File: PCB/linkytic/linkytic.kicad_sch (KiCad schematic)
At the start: 14 parts, among them U1 M5333B, U2 cc2530

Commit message: v0
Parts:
- removed C? (x2): 27pF, Capacitor_SMD:C_0603_1608Metric, symbol Device:C
- removed U2: cc2530, Package_DFN_QFN:HVQFN-40-1EP_6x6mm_P0.5mm_EP4.1x4.1mm, symbol cc2530:cc2530
- removed Y?: Crystal_GND24, symbol Device:Crystal_GND24
- added JP?: Jumper_2_Open, symbol Jumper:Jumper_2_Open
- added U?: CC_debugger, Connector_IDC:IDC-Header_2x05_P2.54mm_Vertical, symbol cc_debugger:CC_debugger
- added U?: E18-MS1-PCB, RF_Module:E18-MS1-PCB, symbol RF_Module:E18-MS1-PCB
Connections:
- net 3v3: now also JP?.1 (A)
- net GND: now also U?.1 (GND), U?.1 (GND)
- net at OC?.4, R?.1: now also U?.21 (P0.2)
- new net: JP?.2 (B), U?.2 (VDD), U?.9 (VCC)
- new net: U?.3 (P2.2), U?.3 (debug_clock_P2.2)
- new net: U?.4 (DD_P2.1), U?.4 (P2.1)
- new net: U?.24 (~{RESET}), U?.7 (RST)

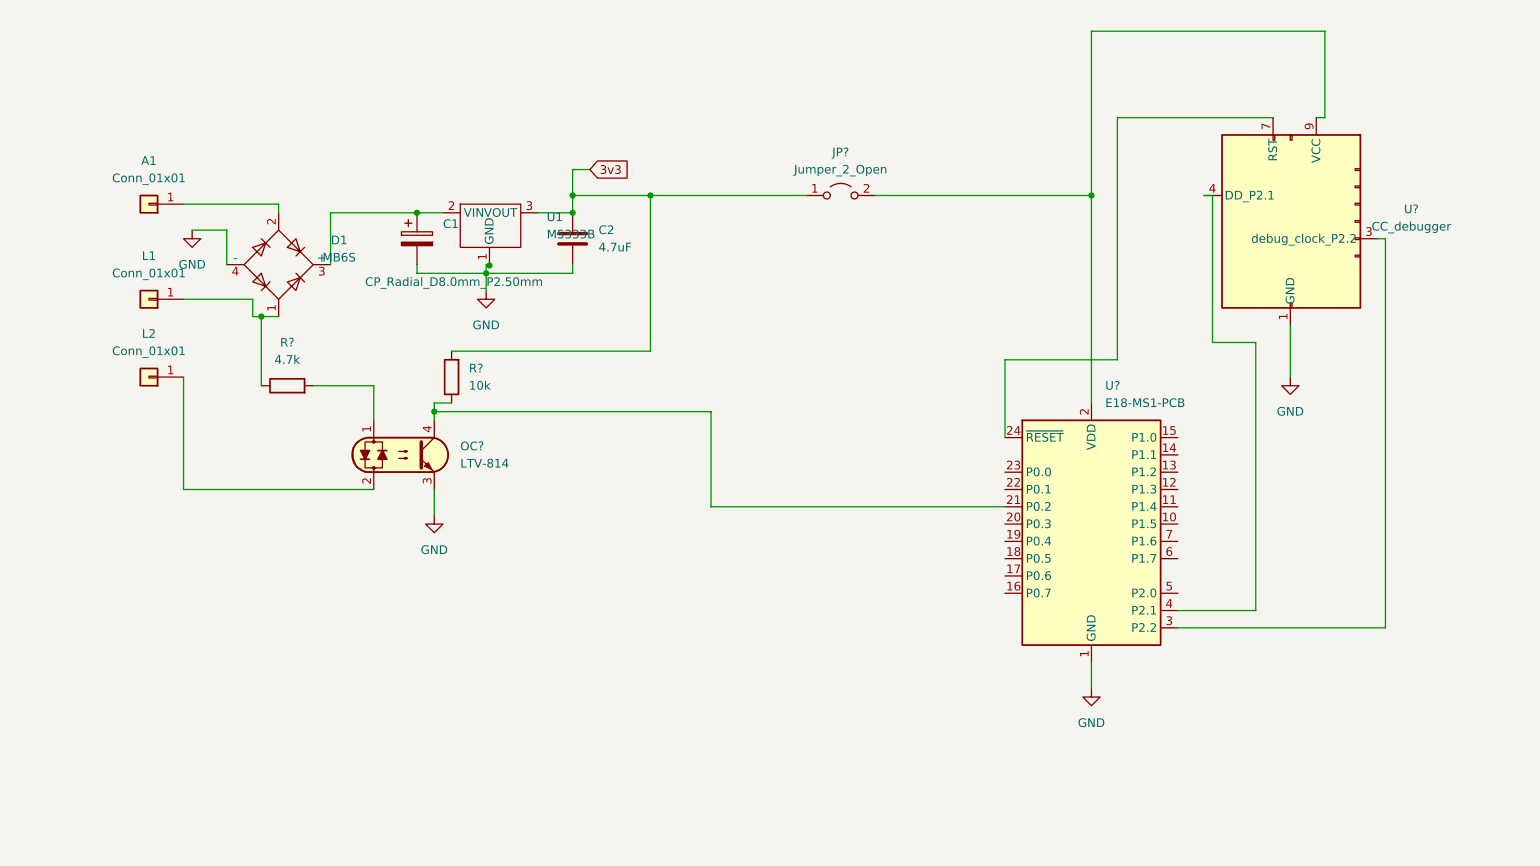
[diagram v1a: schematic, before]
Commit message: Update with thermometre on same board
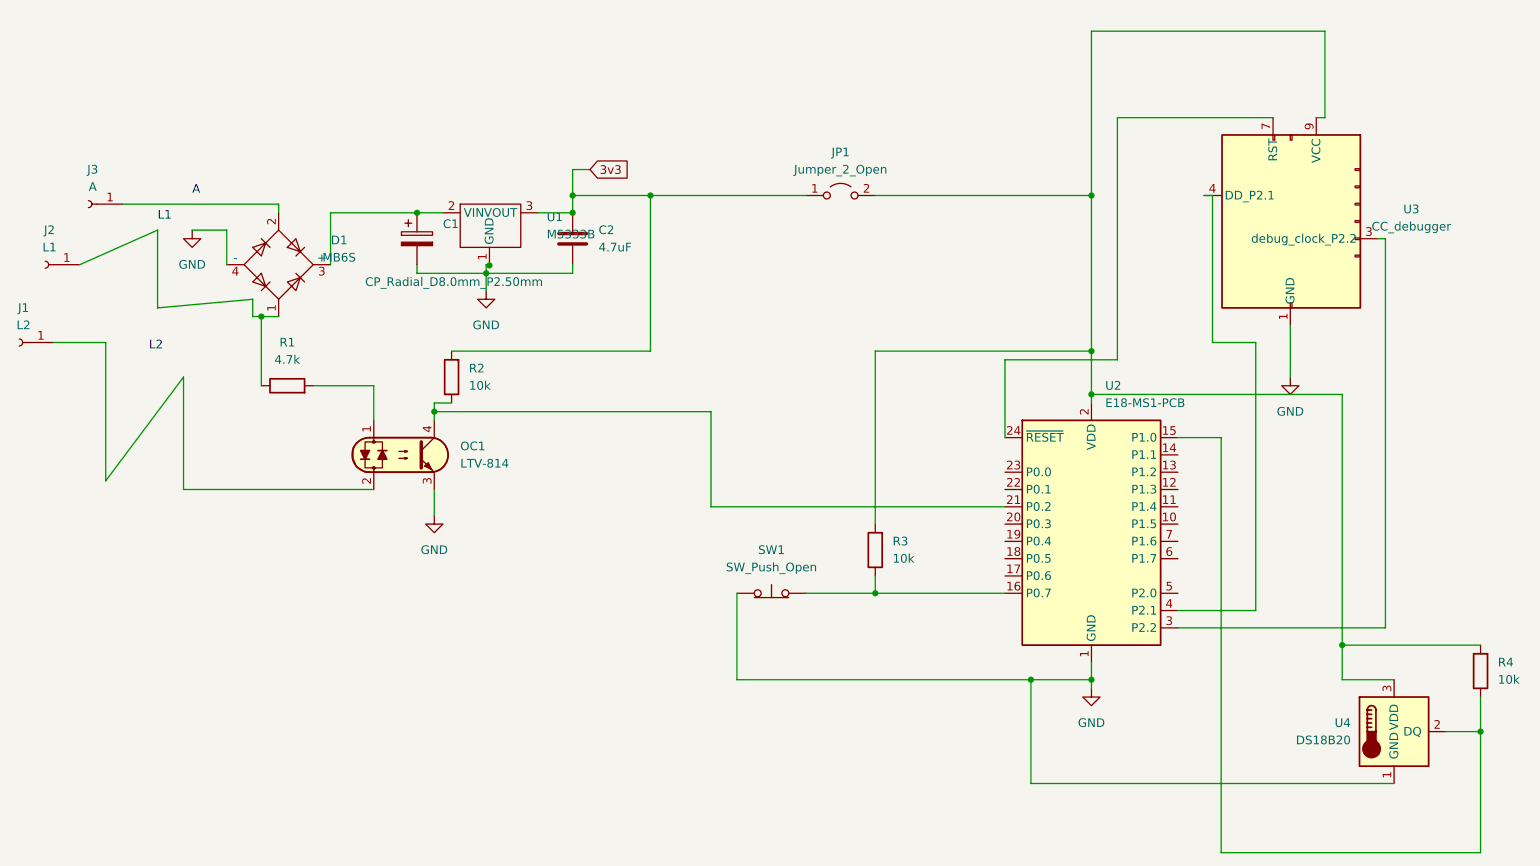
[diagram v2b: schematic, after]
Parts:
- removed A1, L1, L2: Conn_01x01, Connector_Pin:Pin_D1.0mm_L10.0mm, symbol Connector_Generic:Conn_01x01
- added J1: L2, TestPoint:TestPoint_Loop_D2.54mm_Drill1.5mm_Beaded, symbol Connector:Conn_01x01_Female
- added J2: L1, TestPoint:TestPoint_Loop_D2.54mm_Drill1.5mm_Beaded, symbol Connector:Conn_01x01_Female
- added J3: A, TestPoint:TestPoint_Loop_D2.54mm_Drill1.5mm_Beaded, symbol Connector:Conn_01x01_Female
- added R3, R4: 10k, Resistor_SMD:R_0603_1608Metric_Pad0.98x0.95mm_HandSolder, symbol Device:R
- added SW1: SW_Push_Open, Library:interrupteur, symbol Switch:SW_Push_Open
- added U4: DS18B20, Package_TO_SOT_THT:TO-92_Inline, symbol Sensor_Temperature:DS18B20
- JP1: renamed from JP?; footprint (none) -> Jumper_AKL:Jumper_P2.54mm_D0.7mm
- R1, R2: renamed from R?; footprint (none) -> Resistor_SMD:R_0603_1608Metric_Pad0.98x0.95mm_HandSolder
- gave numbers to parts that had none: 3
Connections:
- net GND: now also SW1.1 (A), U4.1 (GND)
- net at D1.1, R1.1: now also J2.1 (Pin_1)
- net at D1.2: now also J3.1 (Pin_1)
- net at JP1.2 (B), U2.2 (VDD), U3.9 (VCC): now also R3.2, R4.2, U4.3 (VDD)
- net at OC1.2: now also J1.1 (Pin_1)
- net at U2.15 (P1.0): now also R4.1, U4.2 (DQ)
- net at U2.16 (P0.7): now also R3.1, SW1.2 (B)
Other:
- note added: "A"
- note added: "L1"
- note added: "L2"

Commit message: first version, that will notwork :/
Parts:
- removed JP1: Jumper_2_Open, Jumper_AKL:Jumper_P2.54mm_D0.7mm, symbol Jumper:Jumper_2_Open
- removed R4: 10k, Resistor_SMD:R_0603_1608Metric_Pad0.98x0.95mm_HandSolder, symbol Device:R
- removed U4: DS18B20, Package_TO_SOT_THT:TO-92_Inline, symbol Sensor_Temperature:DS18B20
- SW1: value SW_Push_Open -> benoit
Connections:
- net 3v3: now also R3.2, U2.2 (VDD), U3.9 (VCC)
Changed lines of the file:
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@@
   (junction (at 213.36 55.88) (diameter 0) (color 0 0 0 0)
   )
-  (junction (at 250.19 121.92) (diameter 0) (color 0 0 0 0)
-  )
-  (junction (at 270.51 134.62) (diameter 0) (color 0 0 0 0)
-  )
   (junction (at 137.16 55.88) (diameter 0) (color 0 0 0 0)
   )
@@
     (stroke (width 0) (type default) (color 0 0 0 0))
   )
-  (wire (pts (xy 270.51 152.4) (xy 232.41 152.4))
-    (stroke (width 0) (type default) (color 0 0 0 0))
-  )
-  (wire (pts (xy 250.19 121.92) (xy 270.51 121.92))
-    (stroke (width 0) (type default) (color 0 0 0 0))
-  )
   (wire (pts (xy 148.59 55.88) (xy 137.16 55.88))
     (stroke (width 0) (type default) (color 0 0 0 0))
@@
     (stroke (width 0) (type default) (color 0 0 0 0))
   )
-  (wire (pts (xy 232.41 91.44) (xy 226.06 91.44))
-    (stroke (width 0) (type default) (color 0 0 0 0))
-  )
-  (wire (pts (xy 80.01 99.06) (xy 80.01 82.55))
-    (stroke (width 0) (type default) (color 0 0 0 0))
-  )
-  (wire (pts (xy 257.81 127) (xy 250.19 127))
-    (stroke (width 0) (type default) (color 0 0 0 0))
-  )
   (wire (pts (xy 116.84 87.63) (xy 157.48 87.63))
     (stroke (width 0) (type default) (color 0 0 0 0))
@@
     (stroke (width 0) (type default) (color 0 0 0 0))
   )
-  (wire (pts (xy 270.51 134.62) (xy 270.51 152.4))
-    (stroke (width 0) (type default) (color 0 0 0 0))
-  )
   (wire (pts (xy 119.38 78.74) (xy 148.59 78.74))
     (stroke (width 0) (type default) (color 0 0 0 0))
@@
     (stroke (width 0) (type default) (color 0 0 0 0))
   )
-  (wire (pts (xy 265.43 134.62) (xy 270.51 134.62))
-    (stroke (width 0) (type default) (color 0 0 0 0))
-  )
   (wire (pts (xy 200.66 80.01) (xy 200.66 91.44))
     (stroke (width 0) (type default) (color 0 0 0 0))
@@
     (stroke (width 0) (type default) (color 0 0 0 0))
   )
-  (wire (pts (xy 76.2 72.39) (xy 90.17 71.12))
-    (stroke (width 0) (type default) (color 0 0 0 0))
-  )
   (wire (pts (xy 114.3 58.42) (xy 118.11 58.42))
     (stroke (width 0) (type default) (color 0 0 0 0))
@@
     (stroke (width 0) (type default) (color 0 0 0 0))
   )
+  (wire (pts (xy 64.77 66.04) (xy 64.77 72.39))
+    (stroke (width 0) (type default) (color 0 0 0 0))
+  )
   (wire (pts (xy 231.14 77.47) (xy 231.14 55.88))
     (stroke (width 0) (type default) (color 0 0 0 0))
   )
-  (wire (pts (xy 270.51 134.62) (xy 270.51 129.54))
-    (stroke (width 0) (type default) (color 0 0 0 0))
-  )
   (wire (pts (xy 181.61 111.76) (xy 181.61 114.3))
     (stroke (width 0) (type default) (color 0 0 0 0))
@@
     (stroke (width 0) (type default) (color 0 0 0 0))
   )
+  (wire (pts (xy 76.2 73.66) (xy 76.2 72.39))
+    (stroke (width 0) (type default) (color 0 0 0 0))
+  )
   (wire (pts (xy 137.16 67.31) (xy 137.16 66.04))
     (stroke (width 0) (type default) (color 0 0 0 0))
   )
-  (wire (pts (xy 90.17 73.66) (xy 91.44 73.66))
+  (wire (pts (xy 76.2 73.66) (xy 91.44 73.66))
     (stroke (width 0) (type default) (color 0 0 0 0))
   )
@@
     (stroke (width 0) (type default) (color 0 0 0 0))
   )
-  (wire (pts (xy 76.2 60.96) (xy 76.2 72.39))
-    (stroke (width 0) (type default) (color 0 0 0 0))
-  )
   (wire (pts (xy 124.46 67.31) (xy 124.46 69.85))
     (stroke (width 0) (type default) (color 0 0 0 0))
   )
-  (wire (pts (xy 148.59 55.88) (xy 171.45 55.88))
-    (stroke (width 0) (type default) (color 0 0 0 0))
-  )
   (wire (pts (xy 204.47 142.24) (xy 204.47 127))
     (stroke (width 0) (type default) (color 0 0 0 0))
@@
     (stroke (width 0) (type default) (color 0 0 0 0))
   )
+  (wire (pts (xy 64.77 72.39) (xy 76.2 72.39))
+    (stroke (width 0) (type default) (color 0 0 0 0))
+  )
   (wire (pts (xy 213.36 31.75) (xy 247.65 31.75))
     (stroke (width 0) (type default) (color 0 0 0 0))
   )
-  (wire (pts (xy 181.61 55.88) (xy 213.36 55.88))
+  (wire (pts (xy 148.59 55.88) (xy 213.36 55.88))
     (stroke (width 0) (type default) (color 0 0 0 0))
   )
@@
     (stroke (width 0) (type default) (color 0 0 0 0))
   )
-  (wire (pts (xy 250.19 127) (xy 250.19 121.92))
-    (stroke (width 0) (type default) (color 0 0 0 0))
-  )
   (wire (pts (xy 139.7 52.07) (xy 137.16 52.07))
     (stroke (width 0) (type default) (color 0 0 0 0))
@@
     (stroke (width 0) (type default) (color 0 0 0 0))
   )
-  (wire (pts (xy 68.58 97.79) (xy 68.58 77.47))
-    (stroke (width 0) (type default) (color 0 0 0 0))
-  )
-  (wire (pts (xy 90.17 71.12) (xy 90.17 73.66))
-    (stroke (width 0) (type default) (color 0 0 0 0))
-  )
-  (wire (pts (xy 250.19 121.92) (xy 250.19 85.09))
+  (wire (pts (xy 68.58 77.47) (xy 68.58 99.06))
     (stroke (width 0) (type default) (color 0 0 0 0))
   )
@@
     (stroke (width 0) (type default) (color 0 0 0 0))
   )
-  (wire (pts (xy 80.01 82.55) (xy 68.58 97.79))
-    (stroke (width 0) (type default) (color 0 0 0 0))
-  )
   (wire (pts (xy 229.87 55.88) (xy 231.14 55.88))
     (stroke (width 0) (type default) (color 0 0 0 0))
@@
     (stroke (width 0) (type default) (color 0 0 0 0))
   )
-  (wire (pts (xy 232.41 152.4) (xy 232.41 91.44))
-    (stroke (width 0) (type default) (color 0 0 0 0))
-  )
-  (wire (pts (xy 64.77 66.04) (xy 76.2 60.96))
-    (stroke (width 0) (type default) (color 0 0 0 0))
-  )
-  (wire (pts (xy 107.95 99.06) (xy 80.01 99.06))
+  (wire (pts (xy 68.58 99.06) (xy 107.95 99.06))
     (stroke (width 0) (type default) (color 0 0 0 0))
   )
@@
   )
   (wire (pts (xy 256.54 62.23) (xy 256.54 119.38))
-    (stroke (width 0) (type default) (color 0 0 0 0))
-  )
-  (wire (pts (xy 257.81 142.24) (xy 204.47 142.24))
     (stroke (width 0) (type default) (color 0 0 0 0))
   )
@@
     (pin "1")
   )
-  (symbol (lib_id "Sensor_Temperature:DS18B20") (at 257.81 134.62 0) (unit 1)
-    (in_bom yes) (on_board yes) (fields_autoplaced)
-    (property "Reference" "U4" (id 0) (at 251.46 133.3499 0)
-      (effects (font (size 1.27 1.27)) (justify right))
-    )
-    (property "Value" "DS18B20" (id 1) (at 251.46 135.8899 0)
-      (effects (font (size 1.27 1.27)) (justify right))
-    )
-    (property "Footprint" "Package_TO_SOT_THT:TO-92_Inline" (id 2) (at 232.41 140.97 0)
-      (effects (font (size 1.27 1.27)) hide)
-    )
-    (property "Datasheet" "http://datasheets.maximintegrated.com/en/ds/DS18B20.pdf" (id 3) (at 254 128.27 0)
-      (effects (font (size 1.27 1.27)) hide)
-    )
-    (pin "1")
-    (pin "2")
-    (pin "3")
-  )
-  (symbol (lib_id "Device:R") (at 270.51 125.73 180) (unit 1)
-    (in_bom yes) (on_board yes) (fields_autoplaced)
-    (property "Reference" "R4" (id 0) (at 273.05 124.4599 0)
-      (effects (font (size 1.27 1.27)) (justify right))
-    )
-    (property "Value" "10k" (id 1) (at 273.05 126.9999 0)
-      (effects (font (size 1.27 1.27)) (justify right))
-    )
-    (property "Footprint" "Resistor_SMD:R_0603_1608Metric_Pad0.98x0.95mm_HandSolder" (id 2) (at 272.288 125.73 90)
-      (effects (font (size 1.27 1.27)) hide)
-    )
-    (property "Datasheet" "~" (id 3) (at 270.51 125.73 0)
-      (effects (font (size 1.27 1.27)) hide)
-    )
-    (pin "1")
-    (pin "2")
-  )
   (symbol (lib_id "Device:C") (at 137.16 62.23 0) (unit 1)
     (in_bom yes) (on_board yes) (fields_autoplaced)
@@
     (in_bom yes) (on_board yes) (fields_autoplaced)
     (property "Reference" "SW1" (id 0) (at 166.37 107.95 0))
-    (property "Value" "SW_Push_Open" (id 1) (at 166.37 110.49 0))
+    (property "Value" "benoit" (id 1) (at 166.37 110.49 0))
     (property "Footprint" "Library:interrupteur" (id 2) (at 166.37 109.22 0)
       (effects (font (size 1.27 1.27)) hide)
@@
     )
     (pin "1")
-  )
-  (symbol (lib_id "Jumper:Jumper_2_Open") (at 176.53 55.88 0) (unit 1)
-    (in_bom yes) (on_board yes) (fields_autoplaced)
-    (property "Reference" "JP1" (id 0) (at 176.53 49.53 0))
-    (property "Value" "Jumper_2_Open" (id 1) (at 176.53 52.07 0))
-    (property "Footprint" "Jumper_AKL:Jumper_P2.54mm_D0.7mm" (id 2) (at 176.53 55.88 0)
-      (effects (font (size 1.27 1.27)) hide)
-    )
-    (property "Datasheet" "~" (id 3) (at 176.53 55.88 0)
-      (effects (font (size 1.27 1.27)) hide)
-    )
-    (pin "1")
-    (pin "2")
   )
   (symbol (lib_id "Connector:Conn_01x01_Female") (at 66.04 57.15 180) (unit 1)
@@
       (reference "J3") (unit 1) (value "A") (footprint "TestPoint:TestPoint_Loop_D2.54mm_Drill1.5mm_Beaded")
     )
-    (path "/5e1c2d48-2a38-427e-99f1-6ab809a0a7cc"
-      (reference "JP1") (unit 1) (value "Jumper_2_Open") (footprint "Jumper_AKL:Jumper_P2.54mm_D0.7mm")
-    )
     (path "/8537eb1f-794f-442f-b8b3-337bf574d542"
       (reference "OC1") (unit 1) (value "LTV-814") (footprint "Package_DIP_AKL:DIP-4_W7.62mm_LongPads")
@@
       (reference "R3") (unit 1) (value "10k") (footprint "Resistor_SMD:R_0603_1608Metric_Pad0.98x0.95mm_HandSolder")
     )
-    (path "/3bea34ab-0e1b-4574-ad2d-5b9e4f63de6e"
-      (reference "R4") (unit 1) (value "10k") (footprint "Resistor_SMD:R_0603_1608Metric_Pad0.98x0.95mm_HandSolder")
-    )
     (path "/44835c60-3552-4bb6-9dc6-e4398896fa08"
-      (reference "SW1") (unit 1) (value "SW_Push_Open") (footprint "Library:interrupteur")
+      (reference "SW1") (unit 1) (value "benoit") (footprint "Library:interrupteur")
     )
     (path "/2255750d-d035-4f4c-9fbb-1f536faa137a"
@@
       (reference "U3") (unit 1) (value "CC_debugger") (footprint "Connector_IDC:IDC-Header_2x05_P2.54mm_Vertical")
     )
-    (path "/32f4f62e-896b-4067-87a6-6ee63f67fbc6"
-      (reference "U4") (unit 1) (value "DS18B20") (footprint "Package_TO_SOT_THT:TO-92_Inline")
-    )
-  )
+  )
